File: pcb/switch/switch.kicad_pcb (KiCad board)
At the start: 2 copper layers, 70.5 x 70.5 mm, 31 parts, among them J1 Conn_01x06, J2 Conn_01x04, J3 Conn_01x05, J4 Conn_01x04, K1 G6SU-2, K2 G6SU-2, K3 G6SU-2, K4 G6SU-2, SW1 D2F-01, SW2 D2F-01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

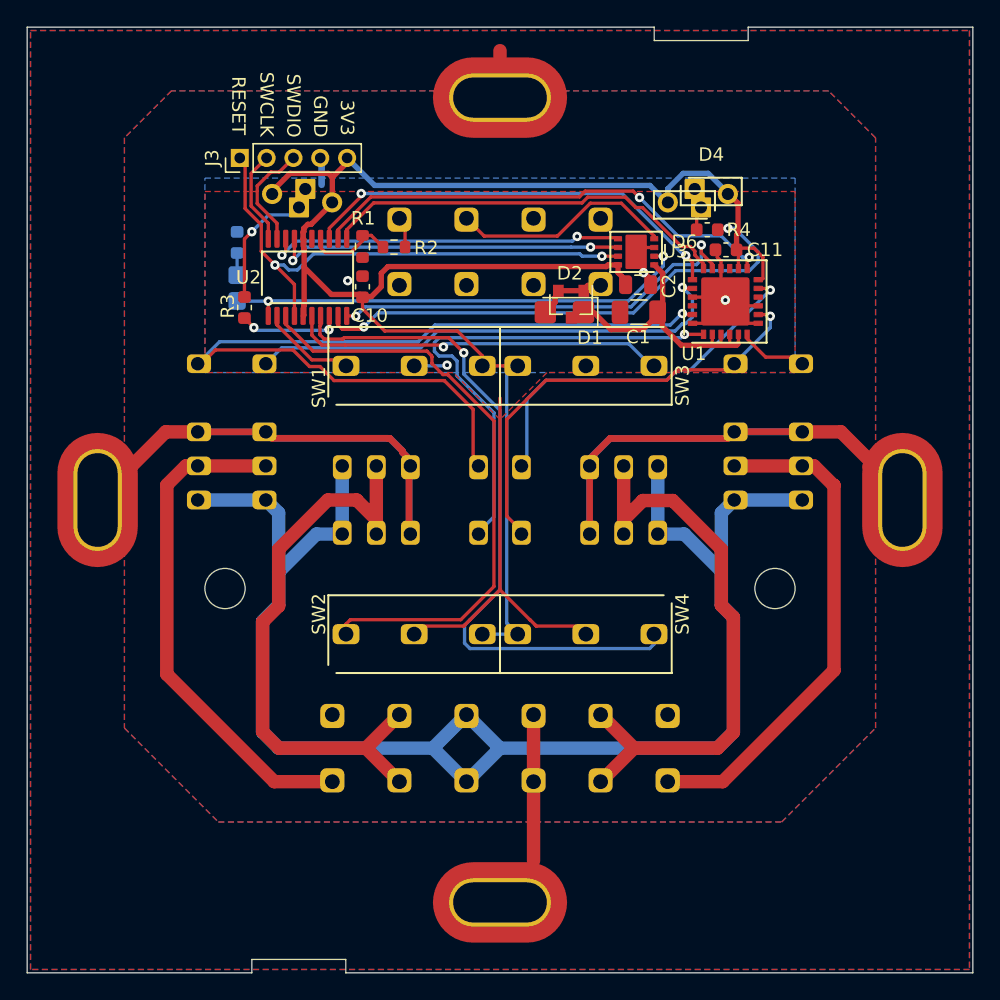
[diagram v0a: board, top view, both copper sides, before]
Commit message: Test circuit for generator, switch: LEDs at center
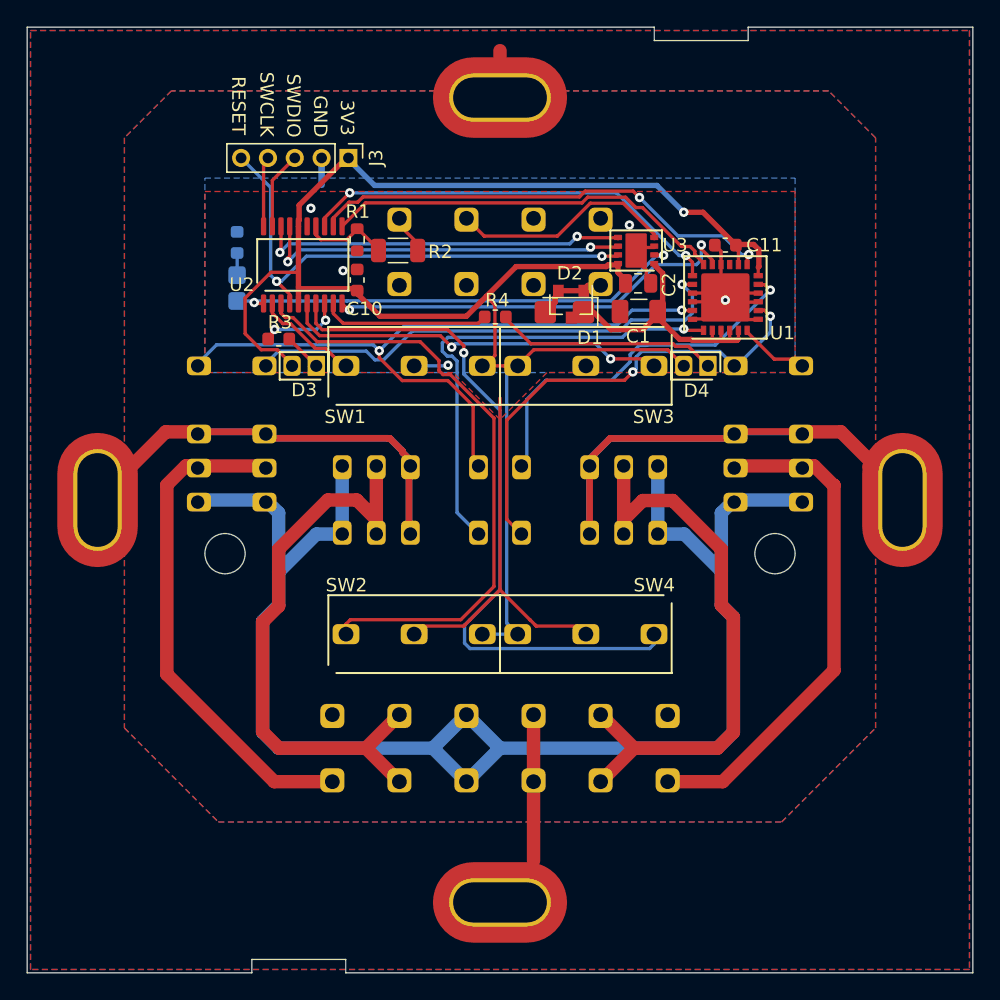
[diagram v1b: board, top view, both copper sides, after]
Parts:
- removed D5, D6: LED, RoomControl:DiodeHolesR
- D2: value D_Schottky_x2_KCom_AAK -> BAS40-05/BAT54C
- D3: footprint RoomControl:DiodeHolesR -> RoomControl:DiodeHolesSwitch; moved to F.Cu
- D4: footprint RoomControl:DiodeHolesR -> RoomControl:DiodeHolesSwitch
- R2: footprint Resistor_SMD:R_0603_1608Metric -> Resistor_SMD:R_1206_3216Metric
- moved R4 17.1 mm to (99.7, 86.3), turned to 180 degrees
- moved D3 13.1 mm to (85.4, 90.0)
- moved D4 13.1 mm to (114.6, 90.0), turned to 180 degrees
- moved J3 8.10 mm to (88.7, 74.5), turned to 270 degrees
- moved R3 3.47 mm to (83.5, 88.0), turned to 180 degrees
- moved U2 0.99 mm to (85.3, 82.5)
- moved C10 0.64 mm to (89.3, 83.6)
- moved R1 0.64 mm to (89.3, 80.6)
- moved R2 0.39 mm to (92.4, 81.4)
- moved C11 0.35 mm to (116.8, 81.0)
- moved U1 0.30 mm to (116.8, 84.9)
- moved K2 0.16 mm to (80.0, 90.0)
- moved K4 0.16 mm to (120.0, 90.0)
- moved C2 0.10 mm to (110.3, 83.8)
- moved U3 0.10 mm to (110.2, 81.4)
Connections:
- J3 pad 1: RESET -> +3V3
- J3 pad 2: SWCLK -> GND
- J3 pad 4: GND -> SWCLK
- J3 pad 5: +3V3 -> RESET
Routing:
- net LEDB: track 38.7 -> 12.9 mm, vias 2 -> 0
- net Net-(D4-Pad1): track 3.10 -> 16.7 mm
- net AY: track 65.7 -> 52.9 mm, vias 1 -> 2
- net +3V3: track 127.5 -> 135.6 mm, vias 0 -> 1
- net Net-(D3-Pad1): track 10.8 -> 3.49 mm, vias 1 -> 0
- net GND: track 46.7 -> 53.3 mm, vias 4 -> 5
- net SWDIO: track 8.12 -> 5.79 mm
- net AX: track 37.5 -> 35.5 mm
- net BY: track 33.3 -> 35.2 mm, vias 1 -> 2
- net SWCLK: track 7.03 -> 5.23 mm
- net +12V: track 21.6 -> 19.9 mm
- net LEDA: track 7.77 -> 6.16 mm
- net SWA0: track 7.30 -> 8.85 mm
- net BUS_TX: track 26.4 -> 27.8 mm
- net SWA1: track 44.7 -> 46.1 mm
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
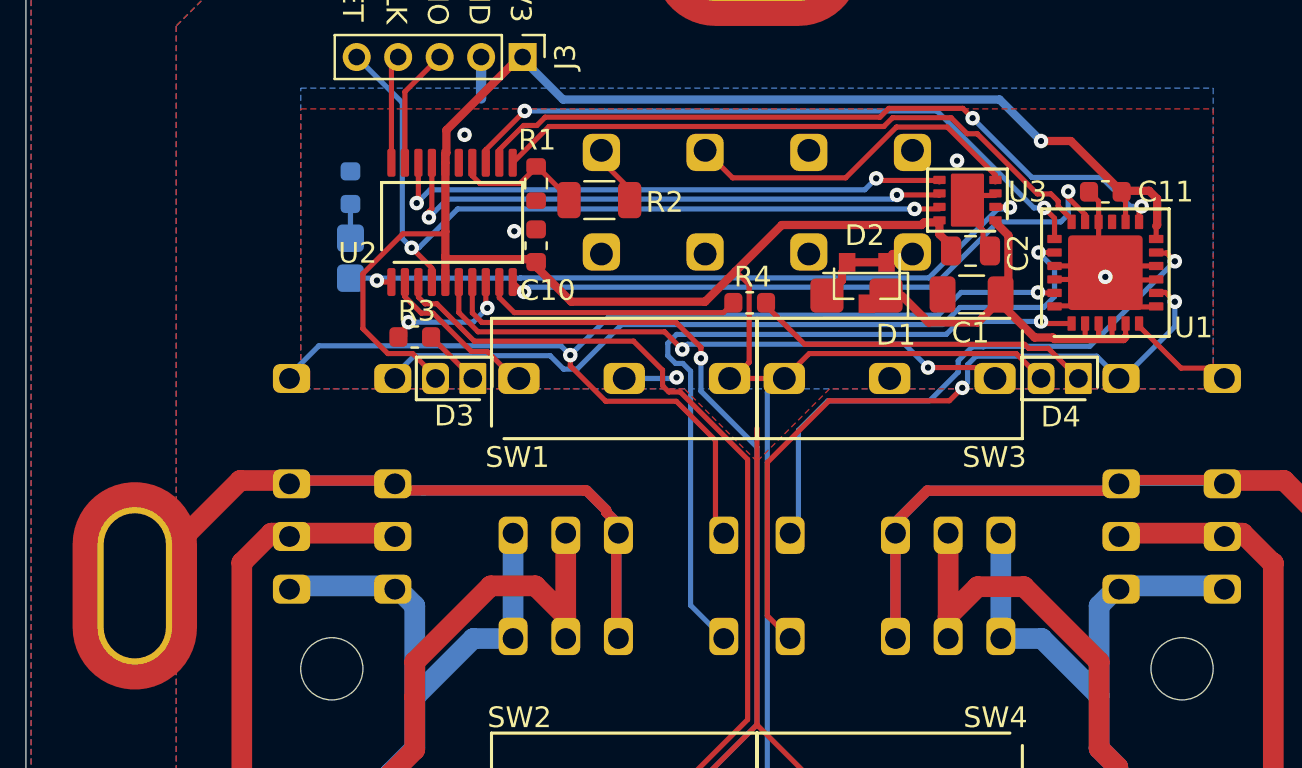
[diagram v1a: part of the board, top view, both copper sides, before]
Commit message: Also update switch to KiCad 6
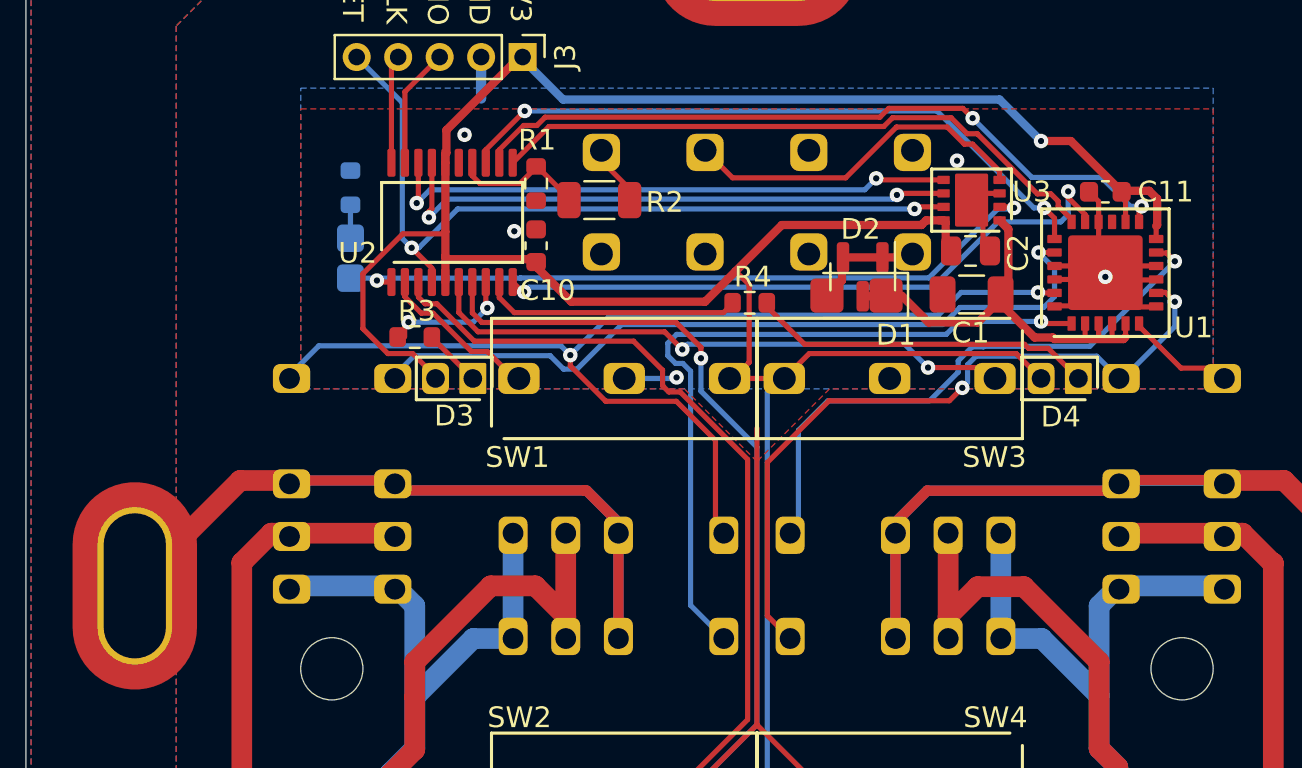
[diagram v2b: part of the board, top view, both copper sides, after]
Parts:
- moved D2 0.36 mm to (105.1, 85.1)
- moved U3 0.20 mm to (110.3, 81.4)
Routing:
- net PE: track 130.1 -> 126.6 mm
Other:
- net class Default removed
- net class Mains removed

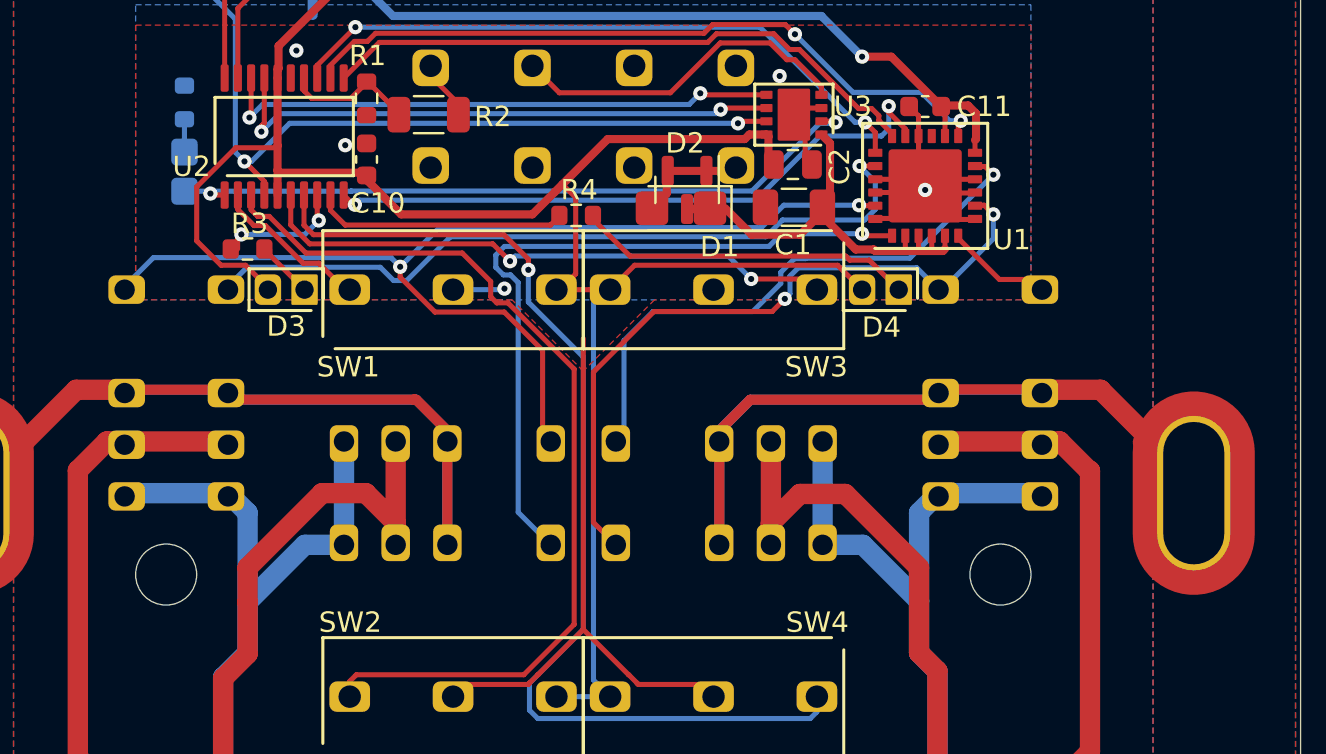
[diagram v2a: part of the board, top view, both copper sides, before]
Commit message: Port symbol library to KiCad 6
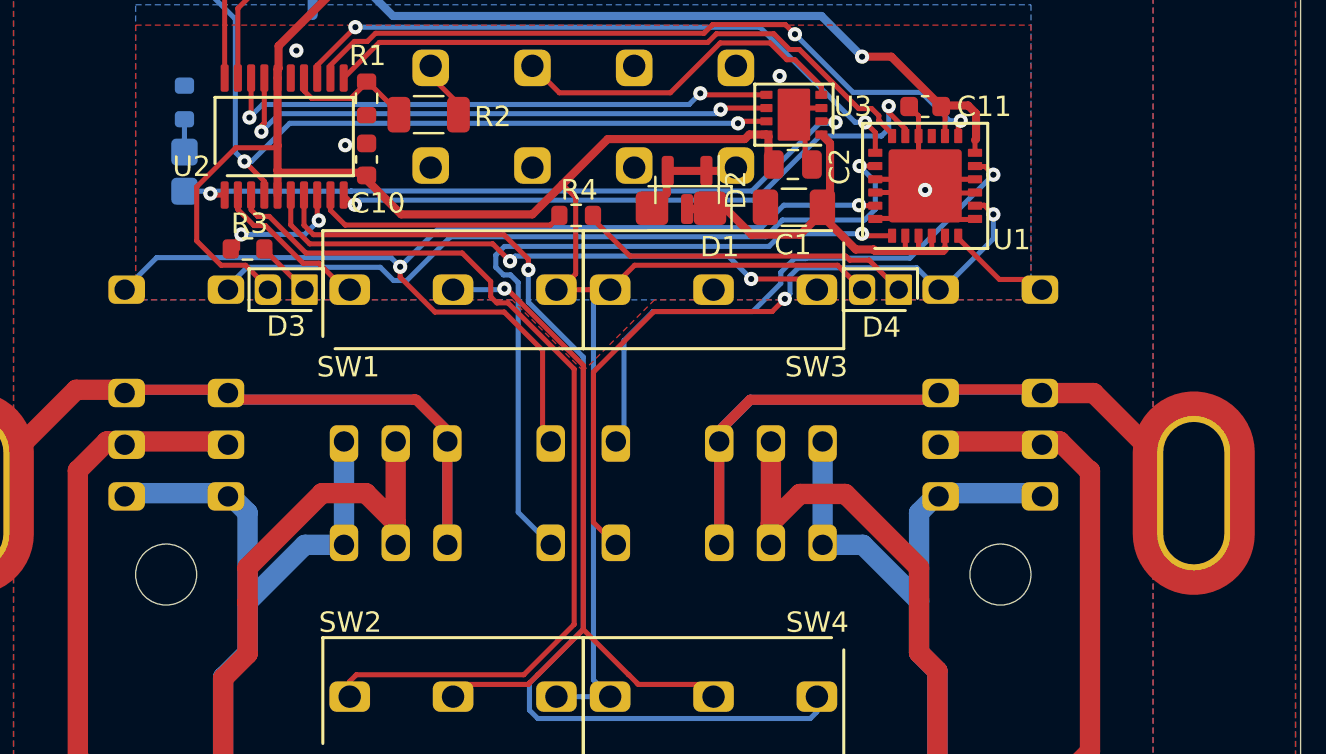
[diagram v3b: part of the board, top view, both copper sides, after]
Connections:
- U1 pad 15: Net-(U1-Pad15) -> unconnected-(U1-Pad15)
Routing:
- net GND: track 53.6 -> 57.8 mm
- net PE: track 126.6 -> 122.7 mm
